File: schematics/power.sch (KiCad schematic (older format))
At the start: 6 parts

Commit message: added protected pn 12V
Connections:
- net +12V renamed +12P
- net -12V renamed -12P
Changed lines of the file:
@@
-EESchema Schematic File Version 2  date Tue 08 Oct 2013 10:14:52 PM EDT
+EESchema Schematic File Version 2  date Tue 08 Oct 2013 10:38:47 PM EDT
 LIBS:power
+LIBS:power_addon
 LIBS:device
 LIBS:transistors
@@
 LIBS:contrib
 LIBS:valves
+LIBS:relays
 LIBS:benchBuddy-cache
 EELAYER 25  0
@@
 $EndDescr
 $Comp
-L -12V #PWR?
-U 1 1 5254B991
+L +12P #PWR?
+U 1 1 5254C19E
+P 7150 1900
+F 0 "#PWR?" H 7150 1870 30  0001 C CNN
+F 1 "+12P" H 7150 2000 30  0000 C CNN
+	1    7150 1900
+	1    0    0    -1
+$EndComp
+$Comp
+L -12P #PWR?
+U 1 1 5254C188
 P 7400 1900
 F 0 "#PWR?" H 7400 2030 20  0001 C CNN
-F 1 "-12V" H 7400 2000 30  0000 C CNN
+F 1 "-12P" H 7400 2000 30  0000 C CNN
 	1    7400 1900
 	1    0    0    -1
@@
 	1    0    0    -1
 $EndComp
-$Comp
-L +12V #PWR?
-U 1 1 5254B947
-P 7150 1900
-F 0 "#PWR?" H 7150 1850 20  0001 C CNN
-F 1 "+12V" H 7150 2000 30  0000 C CNN
-	1    7150 1900
-	1    0    0    -1
-$EndComp

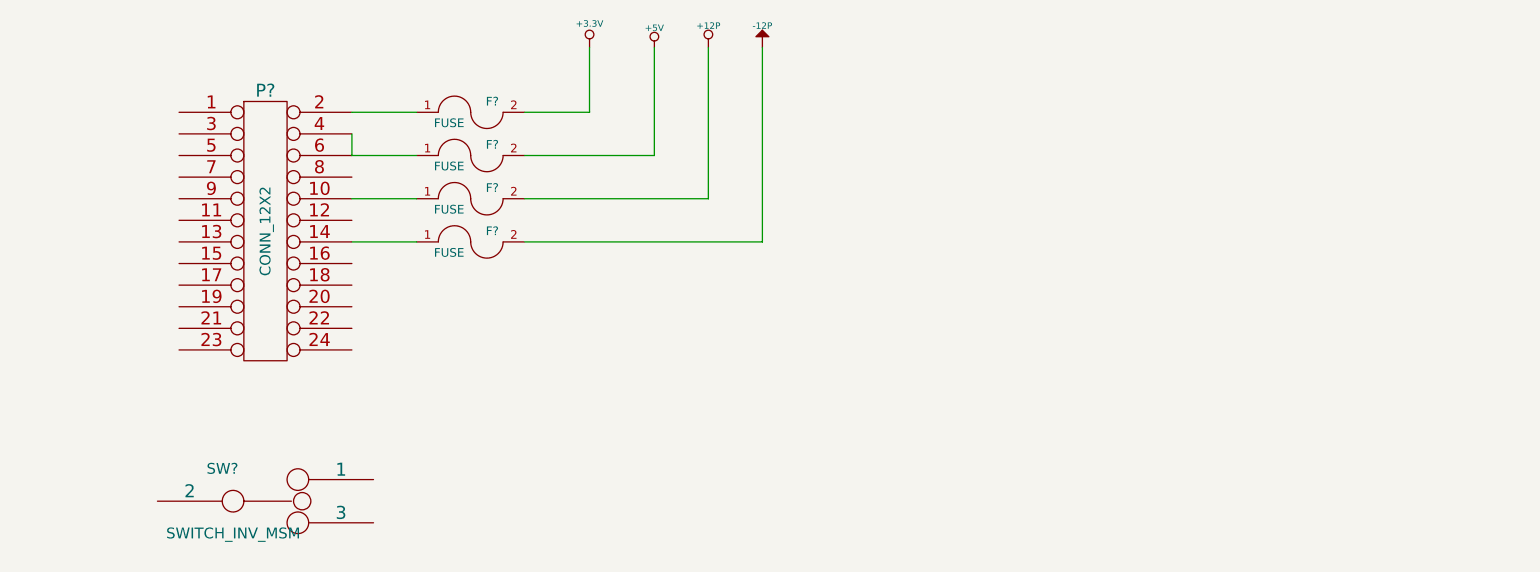
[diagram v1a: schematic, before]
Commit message: addded atx enable switch
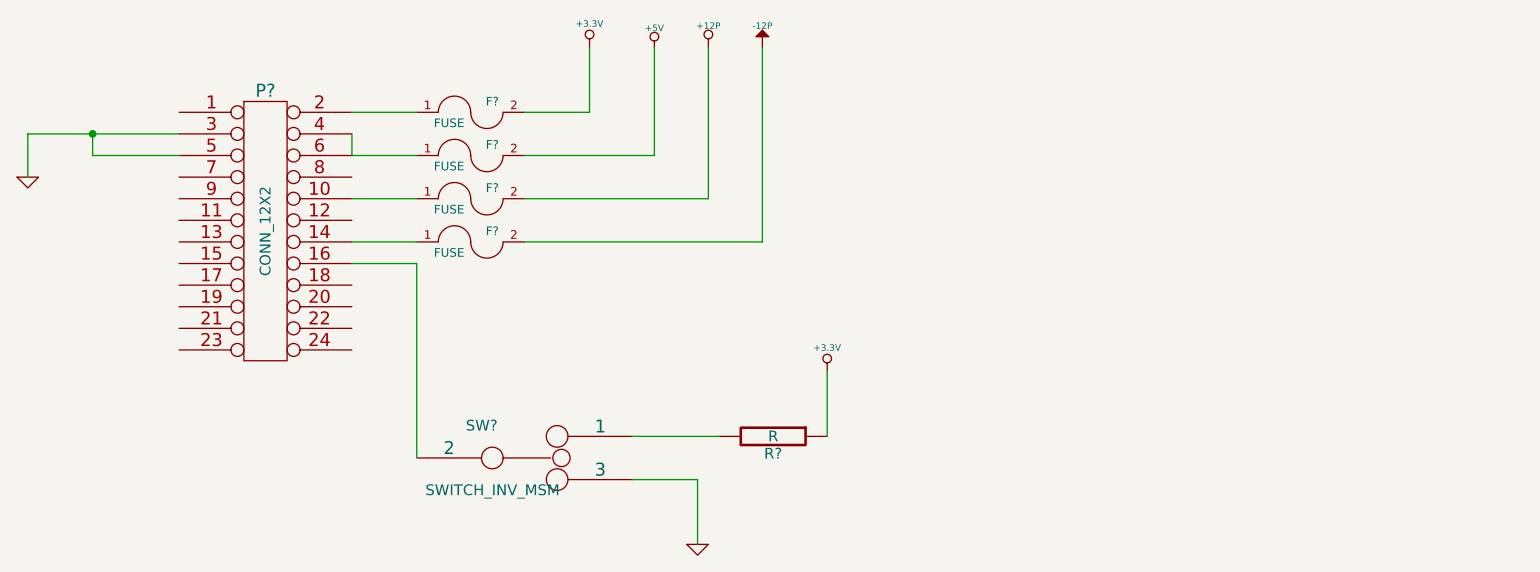
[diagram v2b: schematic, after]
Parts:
- added R?: R, symbol R
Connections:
- net +3.3V: now also R?.1
- net at P?.16 (P16): now also SW?.2
- net GND: now reaches P?.3 (P3)
- net GND: now also P?.5 (P5), SW?.3
- net at SW?.1: now also R?.2
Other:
- moved on the sheet: SW?
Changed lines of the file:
@@
-EESchema Schematic File Version 2  date Tue 08 Oct 2013 10:38:47 PM EDT
+EESchema Schematic File Version 2  date Tue 08 Oct 2013 10:41:11 PM EDT
 LIBS:power
 LIBS:power_addon
@@
 Comment4 ""
 $EndDescr
-$Comp
-L +12P #PWR?
-U 1 1 5254C19E
-P 7150 1900
-F 0 "#PWR?" H 7150 1870 30  0001 C CNN
-F 1 "+12P" H 7150 2000 30  0000 C CNN
-	1    7150 1900
-	1    0    0    -1
-$EndComp
-$Comp
-L -12P #PWR?
-U 1 1 5254C188
-P 7400 1900
-F 0 "#PWR?" H 7400 2030 20  0001 C CNN
-F 1 "-12P" H 7400 2000 30  0000 C CNN
-	1    7400 1900
-	1    0    0    -1
-$EndComp
+Wire Wire Line
+	7700 3700 7700 3400
+Wire Wire Line
+	6800 3900 7100 3900
+Wire Wire Line
+	7100 3900 7100 4200
+Connection ~ 4300 2300
+Wire Wire Line
+	4000 2500 4000 2300
+Wire Wire Line
+	4000 2300 4700 2300
 Wire Wire Line
 	7400 1900 7400 2800
@@
 Wire Wire Line
 	5500 2800 5800 2800
+Wire Wire Line
+	4300 2300 4300 2400
+Wire Wire Line
+	4300 2400 4700 2400
+Wire Wire Line
+	5500 2900 5800 2900
+Wire Wire Line
+	5800 2900 5800 3800
+Wire Wire Line
+	7200 3700 6800 3700
+$Comp
+L +3.3V #PWR?
+U 1 1 5254C23E
+P 7700 3400
+F 0 "#PWR?" H 7700 3360 30  0001 C CNN
+F 1 "+3.3V" H 7700 3510 30  0000 C CNN
+	1    7700 3400
+	1    0    0    -1
+$EndComp
+$Comp
+L R R?
+U 1 1 5254C224
+P 7450 3700
+F 0 "R?" V 7530 3700 50  0000 C CNN
+F 1 "R" V 7450 3700 50  0000 C CNN
+	1    7450 3700
+	0    1    1    0
+$EndComp
+$Comp
+L GND #PWR?
+U 1 1 5254C21C
+P 7100 4200
+F 0 "#PWR?" H 7100 4200 30  0001 C CNN
+F 1 "GND" H 7100 4130 30  0001 C CNN
+	1    7100 4200
+	1    0    0    -1
+$EndComp
+$Comp
+L GND #PWR?
+U 1 1 5254C1F2
+P 4000 2500
+F 0 "#PWR?" H 4000 2500 30  0001 C CNN
+F 1 "GND" H 4000 2430 30  0001 C CNN
+	1    4000 2500
+	1    0    0    -1
+$EndComp
+$Comp
+L +12P #PWR?
+U 1 1 5254C19E
+P 7150 1900
+F 0 "#PWR?" H 7150 1870 30  0001 C CNN
+F 1 "+12P" H 7150 2000 30  0000 C CNN
+	1    7150 1900
+	1    0    0    -1
+$EndComp
+$Comp
+L -12P #PWR?
+U 1 1 5254C188
+P 7400 1900
+F 0 "#PWR?" H 7400 2030 20  0001 C CNN
+F 1 "-12P" H 7400 2000 30  0000 C CNN
+	1    7400 1900
+	1    0    0    -1
+$EndComp
 $Comp
 L FUSE F?
@@
 L SWITCH_INV_MSM SW?
 U 1 1 5254B887
-P 5100 4000
-F 0 "SW?" H 4901 4150 50  0000 C CNN
-F 1 "SWITCH_INV_MSM" H 4951 3851 50  0000 C CNN
-	1    5100 4000
+P 6300 3800
+F 0 "SW?" H 6101 3950 50  0000 C CNN
+F 1 "SWITCH_INV_MSM" H 6151 3651 50  0000 C CNN
+	1    6300 3800
 	1    0    0    -1
 $EndComp

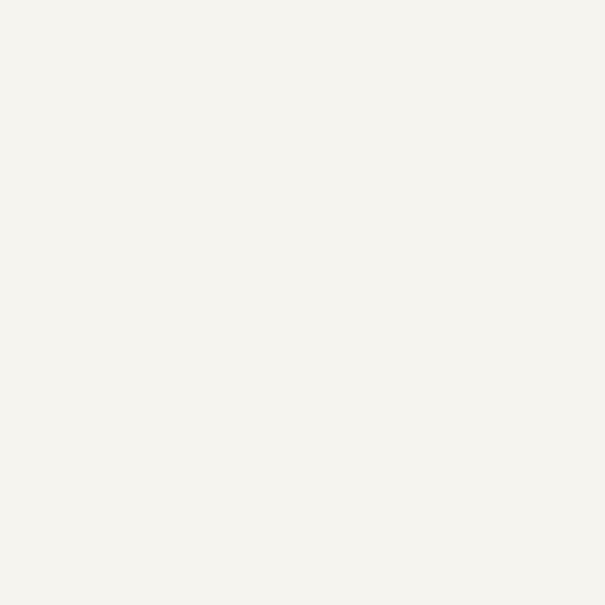
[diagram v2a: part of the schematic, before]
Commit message: added filtering to power
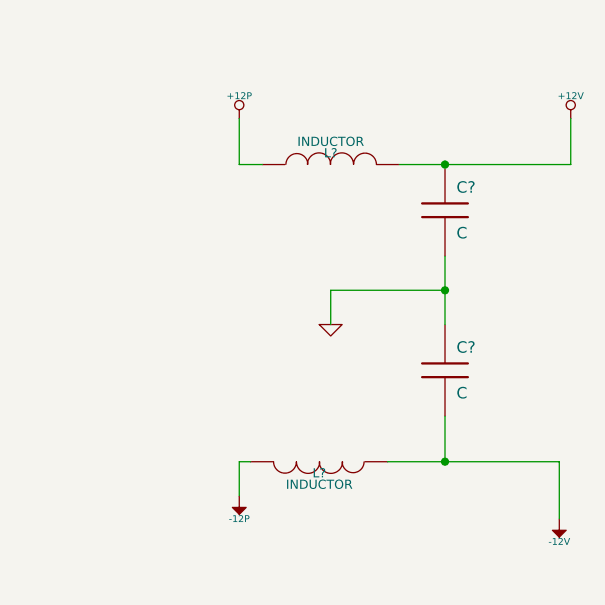
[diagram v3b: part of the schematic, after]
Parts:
- added C? (x2): C, symbol C
- added L? (x2): INDUCTOR, symbol INDUCTOR
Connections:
- net +12P: now also L?.1
- net -12P: now also L?.2
- net GND: now also C?.1, C?.2
- new net +12V: C?.1, L?.2
- new net -12V: C?.2, L?.1
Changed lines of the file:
@@
-EESchema Schematic File Version 2  date Tue 08 Oct 2013 10:41:11 PM EDT
+EESchema Schematic File Version 2  date Tue 08 Oct 2013 10:54:15 PM EDT
 LIBS:power
 LIBS:power_addon
@@
 Comment4 ""
 $EndDescr
+Connection ~ 10300 3700
+Wire Wire Line
+	10050 3700 10800 3700
+Wire Wire Line
+	10800 3700 10800 3950
+Wire Wire Line
+	9800 3100 9800 2950
+Connection ~ 10300 2950
+Wire Wire Line
+	9800 2950 10300 2950
+Wire Wire Line
+	10300 3700 10300 3500
 Wire Wire Line
 	7700 3700 7700 3400
@@
 Wire Wire Line
 	7200 3700 6800 3700
+Wire Wire Line
+	9450 3700 9400 3700
+Wire Wire Line
+	9400 3700 9400 3850
+Wire Wire Line
+	10300 3100 10300 2800
+Wire Wire Line
+	9500 2400 9400 2400
+Wire Wire Line
+	9400 2400 9400 2200
+Wire Wire Line
+	10850 2200 10850 2400
+Wire Wire Line
+	10850 2400 10100 2400
+Connection ~ 10300 2400
+$Comp
+L -12V #PWR?
+U 1 1 5254C377
+P 10800 3950
+F 0 "#PWR?" H 10800 4080 20  0001 C CNN
+F 1 "-12V" H 10800 4050 30  0000 C CNN
+	1    10800 3950
+	-1   0    0    1
+$EndComp
+$Comp
+L +12V #PWR?
+U 1 1 5254C36D
+P 10850 2200
+F 0 "#PWR?" H 10850 2150 20  0001 C CNN
+F 1 "+12V" H 10850 2300 30  0000 C CNN
+	1    10850 2200
+	1    0    0    -1
+$EndComp
+$Comp
+L C C?
+U 1 1 5254C337
+P 10300 3300
+F 0 "C?" H 10350 3400 50  0000 L CNN
+F 1 "C" H 10350 3200 50  0000 L CNN
+	1    10300 3300
+	1    0    0    -1
+$EndComp
+$Comp
+L C C?
+U 1 1 5254C330
+P 10300 2600
+F 0 "C?" H 10350 2700 50  0000 L CNN
+F 1 "C" H 10350 2500 50  0000 L CNN
+	1    10300 2600
+	1    0    0    -1
+$EndComp
+$Comp
+L INDUCTOR L?
+U 1 1 5254C324
+P 9750 3700
+F 0 "L?" V 9800 3700 40  0000 C CNN
+F 1 "INDUCTOR" V 9850 3700 40  0000 C CNN
+	1    9750 3700
+	0    1    1    0
+$EndComp
+$Comp
+L INDUCTOR L?
+U 1 1 5254C311
+P 9800 2400
+F 0 "L?" V 9850 2400 40  0000 C CNN
+F 1 "INDUCTOR" V 9900 2400 40  0000 C CNN
+	1    9800 2400
+	0    -1   -1   0
+$EndComp
+$Comp
+L GND #PWR?
+U 1 1 5254C2F1
+P 9800 3100
+F 0 "#PWR?" H 9800 3100 30  0001 C CNN
+F 1 "GND" H 9800 3030 30  0001 C CNN
+	1    9800 3100
+	1    0    0    -1
+$EndComp
+$Comp
+L -12P #PWR?
+U 1 1 5254C2D3
+P 9400 3850
+F 0 "#PWR?" H 9400 3980 20  0001 C CNN
+F 1 "-12P" H 9400 3950 30  0000 C CNN
+	1    9400 3850
+	-1   0    0    1
+$EndComp
+$Comp
+L +12P #PWR?
+U 1 1 5254C2CD
+P 9400 2200
+F 0 "#PWR?" H 9400 2170 30  0001 C CNN
+F 1 "+12P" H 9400 2300 30  0000 C CNN
+	1    9400 2200
+	1    0    0    -1
+$EndComp
 $Comp
 L +3.3V #PWR?
